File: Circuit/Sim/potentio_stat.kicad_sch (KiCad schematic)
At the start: 18 parts, among them U1 ${SIM.PARAMS}, U2 ${SIM.PARAMS}, U3 ${SIM.PARAMS}, U4 ${SIM.PARAMS}, U5 ${SIM.PARAMS}, U6 ${SIM.PARAMS}, U7 ${SIM.PARAMS}, U8 ${SIM.PARAMS}, U9 ${SIM.PARAMS}

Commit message: 実回路に合わせてシミュレーション回路を調整
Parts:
- removed C1: ${SIM.PARAMS}, symbol Device:C
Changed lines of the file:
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@@
-	)
-	(junction
-		(at 118.11 105.41)
-		(diameter 0)
-		(color 0 0 0 0)
-	)
-	(junction
-		(at 135.89 105.41)
-		(diameter 0)
-		(color 0 0 0 0)
 	)
 	(junction
@@
 	(wire
 		(pts
-			(xy 123.19 93.98) (xy 118.11 93.98)
-		)
-		(stroke
-			(width 0)
-			(type default)
-		)
-	)
-	(wire
-		(pts
-			(xy 135.89 93.98) (xy 130.81 93.98)
-		)
-		(stroke
-			(width 0)
-			(type default)
-		)
-	)
-	(wire
-		(pts
 			(xy 114.3 129.54) (xy 114.3 139.7)
 		)
@@
 	(wire
 		(pts
-			(xy 135.89 105.41) (xy 135.89 93.98)
-		)
-		(stroke
-			(width 0)
-			(type default)
-		)
-	)
-	(wire
-		(pts
 			(xy 24.13 184.15) (xy 24.13 189.23)
-		)
-		(stroke
-			(width 0)
-			(type default)
-		)
-	)
-	(wire
-		(pts
-			(xy 118.11 93.98) (xy 118.11 105.41)
 		)
 		(stroke
@@
 	)
 	(symbol
-		(lib_id "Device:C")
-		(at 127 93.98 90)
-		(unit 1)
-		(exclude_from_sim no)
-		(in_bom yes)
-		(on_board yes)
-		(dnp no)
-		(fields_autoplaced yes)
-		(property "Reference" "C1"
-			(at 127 86.36 90)
-			(effects
-				(font
-					(size 1.27 1.27)
-				)
-			)
-		)
-		(property "Value" "${SIM.PARAMS}"
-			(at 127 88.9 90)
-			(effects
-				(font
-					(size 1.27 1.27)
-				)
-			)
-		)
-		(property "Footprint" ""
-			(at 130.81 93.0148 0)
-			(effects
-				(font
-					(size 1.27 1.27)
-				)
-				(hide yes)
-			)
-		)
-		(property "Datasheet" "~"
-			(at 127 93.98 0)
-			(effects
-				(font
-					(size 1.27 1.27)
-				)
-				(hide yes)
-			)
-		)
-		(property "Description" ""
-			(at 127 93.98 0)
-			(effects
-				(font
-					(size 1.27 1.27)
-				)
-				(hide yes)
-			)
-		)
-		(property "Sim.Device" "C"
-			(at 127 93.98 0)
-			(effects
-				(font
-					(size 1.27 1.27)
-				)
-				(hide yes)
-			)
-		)
-		(property "Sim.Type" "="
-			(at 127 93.98 0)
-			(effects
-				(font
-					(size 1.27 1.27)
-				)
-				(hide yes)
-			)
-		)
-		(property "Sim.Params" "c=1n"
-			(at 127 93.98 0)
-			(effects
-				(font
-					(size 1.27 1.27)
-				)
-				(hide yes)
-			)
-		)
-		(property "Sim.Pins" "1=+ 2=-"
-			(at 127 93.98 0)
-			(effects
-				(font
-					(size 1.27 1.27)
-				)
-				(hide yes)
-			)
-		)
-		(pin "1"
-		)
-		(pin "2"
-		)
-		(instances
-			(project "potentio_stat"
-				(path "/dff053be-d7c3-4dee-8e28-efd05f09390c"
-					(reference "C1")
-					(unit 1)
-				)
-			)
-		)
-	)
-	(symbol
 		(lib_name "VDC_1")
 		(lib_id "Simulation_SPICE:VDC")
@@
 			)
 		)
-		(property "Sim.Params" "pwl=\"0 0 5m 3.3\""
+		(property "Sim.Params" "dc=0 ampl=1 f=1k"
 			(at 27.94 181.61 0)
 			(effects
@@
 			)
 		)
-		(property "Sim.Type" "PWL"
+		(property "Sim.Type" "SIN"
 			(at 24.13 179.07 0)
 			(effects

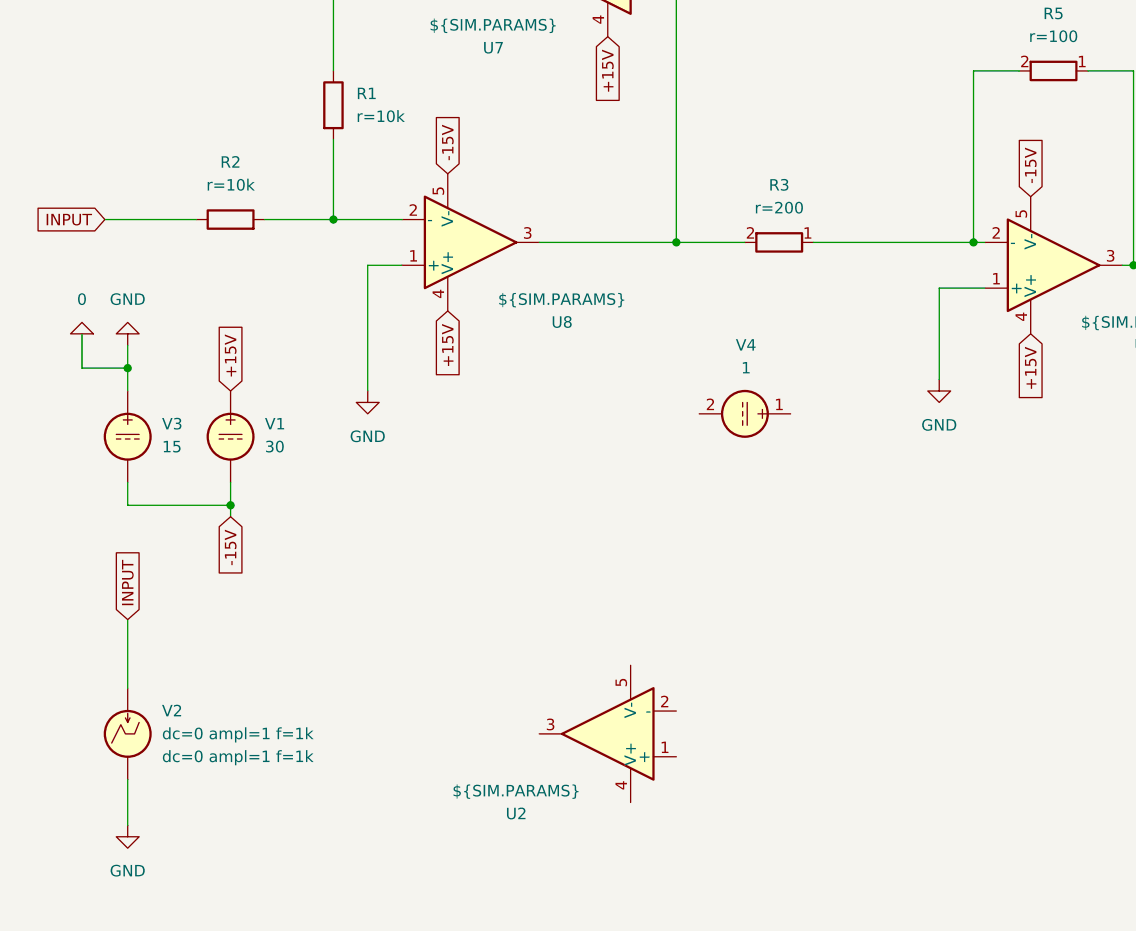
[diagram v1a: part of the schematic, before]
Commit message: SMUのプリント基板回路図完成
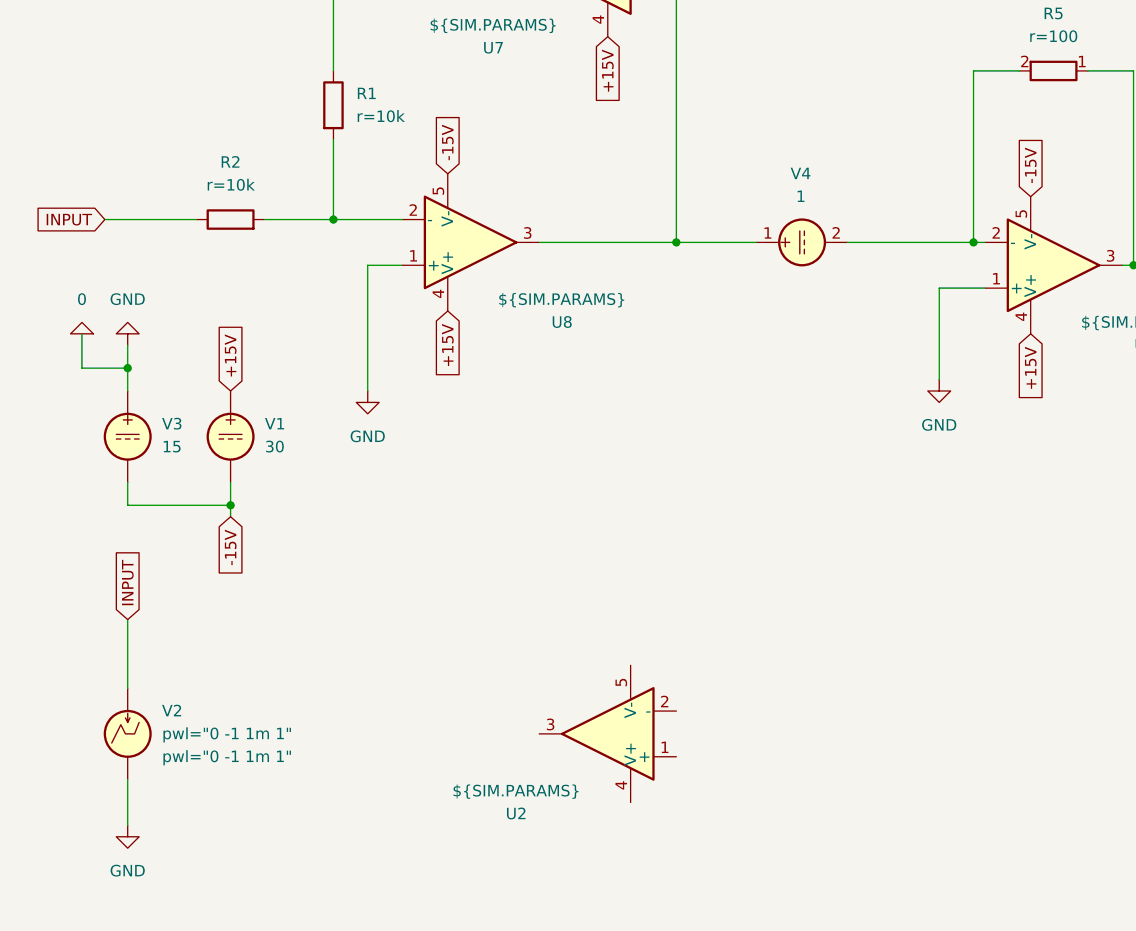
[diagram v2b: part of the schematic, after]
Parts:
- removed R3: ${SIM.PARAMS}, symbol Device:R
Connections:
- net at U7.1 (+), U8.3: now also V4.1
- net at R5.2, U9.2 (-): now also V4.2
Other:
- moved on the sheet: V4
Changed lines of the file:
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@@
 	(wire
 		(pts
-			(xy 100.33 124.46) (xy 118.11 124.46)
+			(xy 104.14 124.46) (xy 118.11 124.46)
 		)
 		(stroke
@@
 	(wire
 		(pts
-			(xy 85.09 124.46) (xy 92.71 124.46)
+			(xy 85.09 124.46) (xy 93.98 124.46)
 		)
 		(stroke
@@
 		(lib_name "VDC_1")
 		(lib_id "Simulation_SPICE:VDC")
-		(at 92.71 143.51 270)
+		(at 99.06 124.46 90)
+		(mirror x)
 		(unit 1)
-		(exclude_from_sim yes)
+		(exclude_from_sim no)
 		(in_bom yes)
 		(on_board yes)
 		(dnp no)
-		(fields_autoplaced yes)
 		(property "Reference" "V4"
-			(at 92.8398 135.89 90)
+			(at 98.9302 116.84 90)
 			(effects
 				(font
@@
 		)
 		(property "Value" "1"
-			(at 92.8398 138.43 90)
+			(at 98.9302 119.38 90)
 			(effects
 				(font
@@
 		)
 		(property "Footprint" ""
-			(at 92.71 143.51 0)
+			(at 99.06 124.46 0)
 			(effects
 				(font
@@
 		)
 		(property "Datasheet" "~"
-			(at 92.71 143.51 0)
+			(at 99.06 124.46 0)
 			(effects
 				(font
@@
 		)
 		(property "Description" ""
-			(at 92.71 143.51 0)
+			(at 99.06 124.46 0)
 			(effects
 				(font
@@
 		)
 		(property "Sim.Device" "SUBCKT"
-			(at 92.71 143.51 0)
+			(at 99.06 124.46 0)
 			(effects
 				(font
@@
 		)
 		(property "Sim.Library" "solar.lib"
-			(at 92.71 143.51 0)
+			(at 99.06 124.46 0)
 			(effects
 				(font
@@
 		)
 		(property "Sim.Name" "Cell"
-			(at 92.71 143.51 0)
+			(at 99.06 124.46 0)
 			(effects
 				(font
@@
 		)
 		(property "Sim.Pins" "1=V+ 2=V-"
-			(at 92.71 143.51 0)
+			(at 99.06 124.46 0)
 			(effects
 				(font
@@
 	)
 	(symbol
-		(lib_name "R_1")
-		(lib_id "Device:R")
-		(at 96.52 124.46 270)
-		(unit 1)
-		(exclude_from_sim no)
-		(in_bom yes)
-		(on_board yes)
-		(dnp no)
-		(fields_autoplaced yes)
-		(property "Reference" "R3"
-			(at 96.52 118.11 90)
-			(effects
-				(font
-					(size 1.27 1.27)
-				)
-			)
-		)
-		(property "Value" "${SIM.PARAMS}"
-			(at 96.52 120.65 90)
-			(effects
-				(font
-					(size 1.27 1.27)
-				)
-			)
-		)
-		(property "Footprint" ""
-			(at 96.52 122.682 90)
-			(effects
-				(font
-					(size 1.27 1.27)
-				)
-				(hide yes)
-			)
-		)
-		(property "Datasheet" "~"
-			(at 96.52 124.46 0)
-			(effects
-				(font
-					(size 1.27 1.27)
-				)
-				(hide yes)
-			)
-		)
-		(property "Description" ""
-			(at 96.52 124.46 0)
-			(effects
-				(font
-					(size 1.27 1.27)
-				)
-				(hide yes)
-			)
-		)
-		(property "Sim.Device" "R"
-			(at 96.52 124.46 0)
-			(effects
-				(font
-					(size 1.27 1.27)
-				)
-				(hide yes)
-			)
-		)
-		(property "Sim.Type" "="
-			(at 96.52 124.46 0)
-			(effects
-				(font
-					(size 1.27 1.27)
-				)
-				(hide yes)
-			)
-		)
-		(property "Sim.Params" "r=200"
-			(at 96.52 124.46 0)
-			(effects
-				(font
-					(size 1.27 1.27)
-				)
-				(hide yes)
-			)
-		)
-		(property "Sim.Pins" "1=+ 2=-"
-			(at 96.52 124.46 0)
-			(effects
-				(font
-					(size 1.27 1.27)
-				)
-				(hide yes)
-			)
-		)
-		(pin "1"
-		)
-		(pin "2"
-		)
-		(instances
-			(project "potentio_stat"
-				(path "/dff053be-d7c3-4dee-8e28-efd05f09390c"
-					(reference "R3")
-					(unit 1)
-				)
-			)
-		)
-	)
-	(symbol
 		(lib_id "Simulation_SPICE:IPWL")
 		(at 24.13 179.07 0)
@@
 			)
 		)
-		(property "Sim.Params" "dc=0 ampl=1 f=1k"
+		(property "Sim.Params" "pwl=\"0 -1 1m 1\""
 			(at 27.94 181.61 0)
 			(effects
@@
 			)
 		)
-		(property "Sim.Type" "SIN"
+		(property "Sim.Type" "PWL"
 			(at 24.13 179.07 0)
 			(effects

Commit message: 電気化学インピーダンス用アップデート
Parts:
- removed V4: 1, symbol Simulation_SPICE:VDC
- added C1: ${SIM.PARAMS}, symbol Device:C
- added R3, R4, R6: ${SIM.PARAMS}, symbol Device:R
- added V4, V6: VPULSE, symbol Simulation_SPICE:VPULSE
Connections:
- net +15V: now also U1.4 (V+), U3.4 (V+), U4.4 (V+); no longer U7.4 (V+), U8.4 (V+), U9.4 (V+)
- net -15V: now also U1.5 (V-), U3.5 (V-), U4.5 (V-); no longer U7.5 (V-), U8.5 (V-), U9.5 (V-)
- net 0: now also U3.1 (+), U4.1 (+), V4.2, V6.2; no longer U8.1 (+), U9.1 (+)
- net INPUT: now also V4.1, V6.1
- net Vcrr: now also R5.2, U4.3; no longer R5.1, U9.3
- net Vre: now also U1.2 (-), U1.3; no longer U7.2 (-), U7.3
- net at U4.2 (-): now also R5.1, C1.2, R3.1
- net at U7.1 (+): no longer U8.3
- net at U9.2 (-): no longer R5.2
- net at R1.2, R2.2: now also U3.2 (-); no longer U8.2 (-)
- net at U3.3: now also U1.1 (+), R6.2
- new net: C1.1, R3.2, R4.1
- new net: R4.2, R6.1
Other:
- moved on the sheet: R1, R2, R5, U1, U3, U4, V1, V2, V3
